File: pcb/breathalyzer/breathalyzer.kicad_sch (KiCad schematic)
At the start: 29 parts, among them J1 Conn_01x07_Pin, J2 MP-3B socket, Q1 Q_PMOS, Q2 NPN, SW1 PTS636SK43SMTR, SW2 430162085826, U1 STM32F030K6Tx, U2 TLV73325PDBV, U4 TLV61070ADBV, U5 AY0438X-L

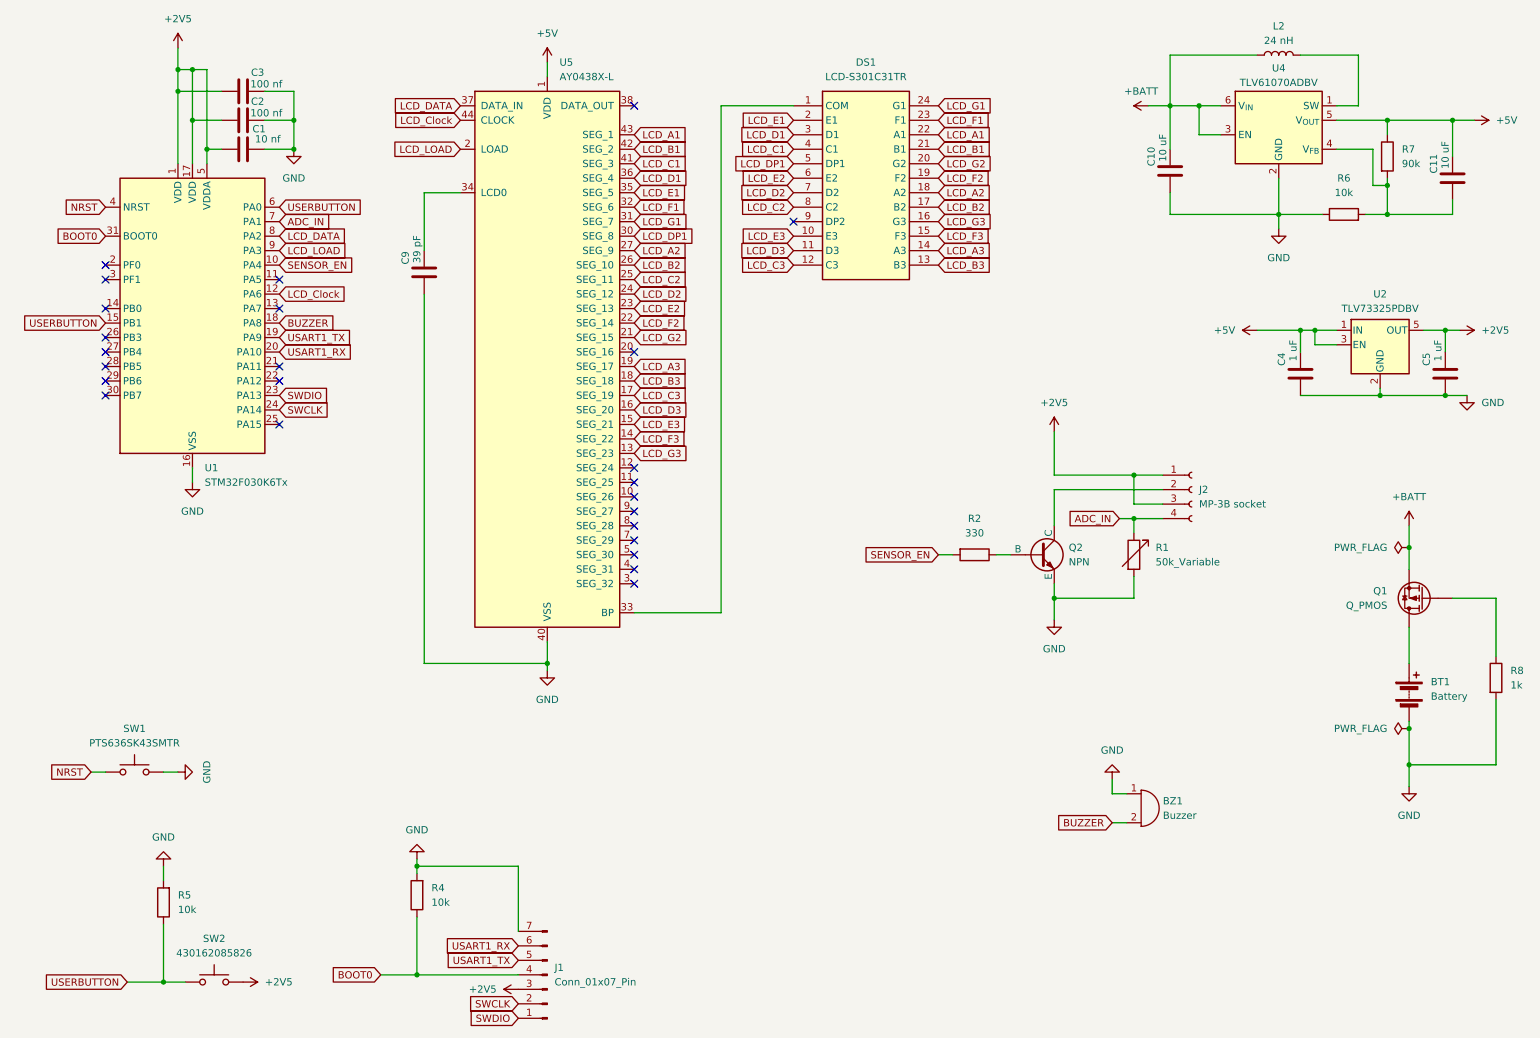
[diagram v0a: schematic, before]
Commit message: update from schematic
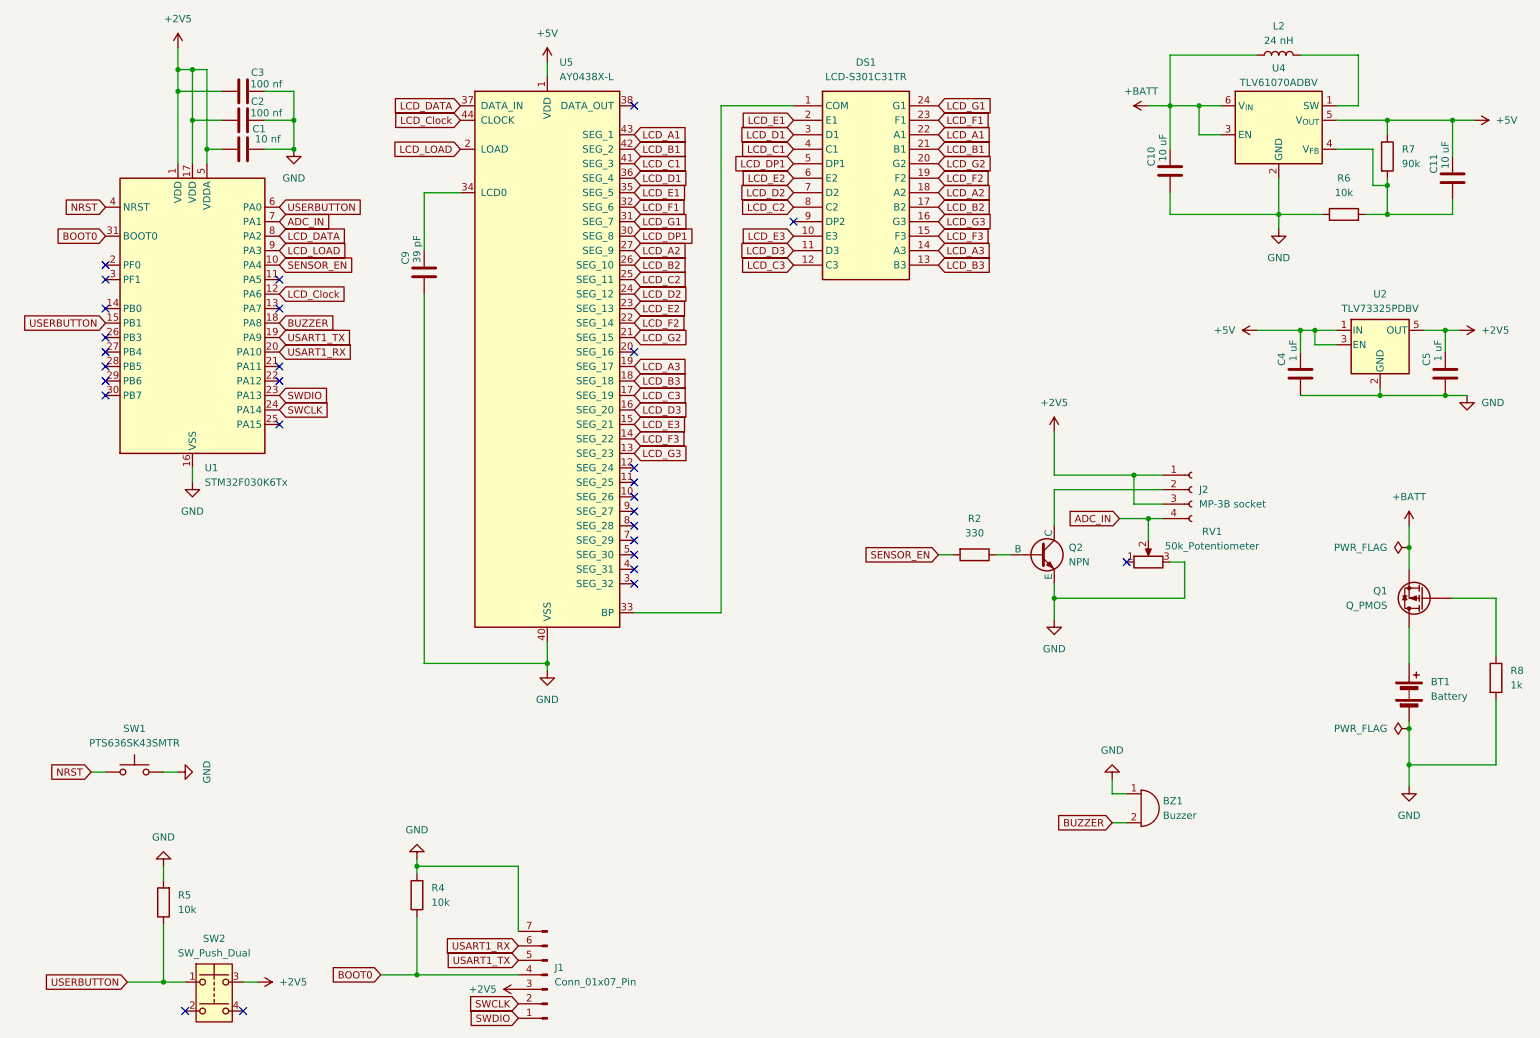
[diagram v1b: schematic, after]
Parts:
- removed R1: 50k_Variable, Potentiometer_THT:Potentiometer_ACP_CA9-H5_Horizontal, symbol Device:R_Variable
- removed SW2: 430162085826, breathalyzer:430162085826, symbol Switch:SW_Push
- added RV1: 50k_Potentiometer, Potentiometer_THT:Potentiometer_ACP_CA9-H5_Horizontal, symbol Device:R_Potentiometer
- added SW2: SW_Push_Dual, breathalyzer:430162085826, symbol Switch:SW_Push_Dual
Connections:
- net +2V5: now also SW2.3
- net ADC_IN: now also RV1.2
- net GND: now also RV1.3
- net USERBUTTON: now also SW2.1
- no-connect marks 25 -> 28
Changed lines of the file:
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@@
 	)
 	(junction
-		(at 209.55 101.6)
-		(diameter 0)
-		(color 0 0 0 0)
-	)
-	(junction
 		(at 254 48.26)
 		(diameter 0)
@@
 		(color 0 0 0 0)
 	)
+	(junction
+		(at 212.09 101.6)
+		(diameter 0)
+		(color 0 0 0 0)
+	)
 	(no_connect
 		(at 121.92 110.49)
@@
 	)
 	(no_connect
+		(at 208.28 109.22)
+	)
+	(no_connect
 		(at 121.92 113.03)
 	)
@@
 	)
 	(no_connect
+		(at 43.18 187.96)
+	)
+	(no_connect
 		(at 59.69 85.09)
 	)
@@
 	)
 	(no_connect
+		(at 53.34 187.96)
+	)
+	(no_connect
 		(at 29.21 74.93)
 	)
@@
 	(wire
 		(pts
+			(xy 218.44 109.22) (xy 218.44 115.57)
+		)
+		(stroke
+			(width 0)
+			(type default)
+		)
+	)
+	(wire
+		(pts
 			(xy 46.99 36.83) (xy 49.53 36.83)
 		)
@@
 	(wire
 		(pts
-			(xy 214.63 101.6) (xy 209.55 101.6)
+			(xy 207.01 101.6) (xy 212.09 101.6)
 		)
 		(stroke
@@
 	(wire
 		(pts
-			(xy 209.55 101.6) (xy 209.55 104.14)
+			(xy 252.73 78.74) (xy 252.73 80.01)
 		)
 		(stroke
@@
 	(wire
 		(pts
-			(xy 252.73 78.74) (xy 252.73 80.01)
+			(xy 44.45 95.25) (xy 44.45 92.71)
 		)
 		(stroke
@@
 	(wire
 		(pts
-			(xy 44.45 95.25) (xy 44.45 92.71)
+			(xy 266.7 68.58) (xy 264.16 68.58)
 		)
 		(stroke
@@
 	(wire
 		(pts
-			(xy 266.7 68.58) (xy 264.16 68.58)
+			(xy 220.98 34.29) (xy 220.98 29.21)
 		)
 		(stroke
@@
 	(wire
 		(pts
-			(xy 220.98 34.29) (xy 220.98 29.21)
+			(xy 62.23 31.75) (xy 62.23 36.83)
 		)
 		(stroke
@@
 	(wire
 		(pts
-			(xy 62.23 31.75) (xy 62.23 36.83)
+			(xy 212.09 101.6) (xy 214.63 101.6)
 		)
 		(stroke
@@
 	(wire
 		(pts
-			(xy 44.45 31.75) (xy 44.45 39.37)
+			(xy 55.88 182.88) (xy 53.34 182.88)
 		)
 		(stroke
@@
 	(wire
 		(pts
-			(xy 41.91 22.86) (xy 41.91 26.67)
+			(xy 44.45 31.75) (xy 44.45 39.37)
 		)
 		(stroke
@@
 	(wire
 		(pts
-			(xy 83.82 162.56) (xy 101.6 162.56)
+			(xy 218.44 109.22) (xy 215.9 109.22)
 		)
 		(stroke
@@
 	(wire
 		(pts
-			(xy 241.3 71.12) (xy 241.3 68.58)
+			(xy 41.91 22.86) (xy 41.91 26.67)
 		)
 		(stroke
@@
 	(wire
 		(pts
-			(xy 205.74 149.86) (xy 208.28 149.86)
+			(xy 83.82 162.56) (xy 101.6 162.56)
 		)
 		(stroke
@@
 	(wire
 		(pts
-			(xy 39.37 182.88) (xy 43.18 182.88)
+			(xy 241.3 71.12) (xy 241.3 68.58)
 		)
 		(stroke
@@
 	(wire
 		(pts
-			(xy 209.55 111.76) (xy 209.55 115.57)
+			(xy 205.74 149.86) (xy 208.28 149.86)
 		)
 		(stroke
@@
 	(wire
 		(pts
-			(xy 83.82 161.29) (xy 83.82 162.56)
+			(xy 39.37 182.88) (xy 43.18 182.88)
 		)
 		(stroke
@@
 	(wire
 		(pts
-			(xy 209.55 115.57) (xy 195.58 115.57)
+			(xy 83.82 161.29) (xy 83.82 162.56)
 		)
 		(stroke
@@
 	(wire
 		(pts
-			(xy 195.58 115.57) (xy 195.58 119.38)
+			(xy 195.58 115.57) (xy 218.44 115.57)
 		)
 		(stroke
@@
 	(wire
 		(pts
-			(xy 207.01 101.6) (xy 209.55 101.6)
+			(xy 195.58 115.57) (xy 195.58 119.38)
 		)
 		(stroke
@@
 	(wire
 		(pts
+			(xy 212.09 101.6) (xy 212.09 105.41)
+		)
+		(stroke
+			(width 0)
+			(type default)
+		)
+	)
+	(wire
+		(pts
 			(xy 62.23 26.67) (xy 62.23 31.75)
 		)
@@
 	(symbol
 		(lib_id "power:+2V5")
-		(at 53.34 182.88 270)
+		(at 55.88 182.88 270)
 		(unit 1)
 		(exclude_from_sim no)
@@
 		(fields_autoplaced yes)
 		(property "Reference" "#PWR010"
-			(at 49.53 182.88 0)
+			(at 52.07 182.88 0)
 			(effects
 				(font
@@
 		)
 		(property "Value" "+2V5"
-			(at 57.15 182.8799 90)
+			(at 59.69 182.8799 90)
 			(effects
 				(font
@@
 		)
 		(property "Footprint" ""
-			(at 53.34 182.88 0)
+			(at 55.88 182.88 0)
 			(effects
 				(font
@@
 		)
 		(property "Datasheet" ""
-			(at 53.34 182.88 0)
+			(at 55.88 182.88 0)
 			(effects
 				(font
@@
 		)
 		(property "Description" "Power symbol creates a global label with name \"+2V5\""
-			(at 53.34 182.88 0)
+			(at 55.88 182.88 0)
 			(effects
 				(font
@@
 	)
 	(symbol
-		(lib_name "SW_Push_1")
-		(lib_id "Switch:SW_Push")
-		(at 48.26 182.88 0)
+		(lib_id "Device:R_Potentiometer")
+		(at 212.09 109.22 90)
 		(unit 1)
 		(exclude_from_sim no)
@@
 		(on_board yes)
 		(dnp no)
-		(fields_autoplaced yes)
-		(property "Reference" "SW2"
-			(at 48.26 175.26 0)
+		(property "Reference" "RV1"
+			(at 223.266 103.886 90)
 			(effects
 				(font
@@
 			)
 		)
-		(property "Value" "430162085826"
-			(at 48.26 177.8 0)
+		(property "Value" "50k_Potentiometer"
+			(at 223.266 106.426 90)
 			(effects
 				(font
@@
 			)
 		)
-		(property "Footprint" "breathalyzer:430162085826"
-			(at 48.26 177.8 0)
+		(property "Footprint" "Potentiometer_THT:Potentiometer_ACP_CA9-H5_Horizontal"
+			(at 212.09 109.22 0)
 			(effects
 				(font
@@
 			)
 		)
-		(property "Datasheet" "https://hu.mouser.com/ProductDetail/Wurth-Elektronik/430162085826?qs=sPbYRqrBIVnNOZ1%252Bx8%2F2Rw%3D%3D"
-			(at 48.26 177.8 0)
+		(property "Datasheet" "https://hu.mouser.com/ProductDetail/Same-Sky/PTN06-B50CB20-H?qs=sGAEpiMZZMu7u4aXTvZ%252Bj76JCkJt%2F1Rf8NnkN%252BqUlJ17HNc3pPYO6w%3D%3D"
+			(at 212.09 109.22 0)
 			(effects
 				(font
@@
 			)
 		)
-		(property "Description" "Push button switch, generic, two pins"
-			(at 48.26 182.88 0)
+		(property "Description" "Potentiometer"
+			(at 212.09 109.22 0)
 			(effects
 				(font
@@
 			)
 		)
-		(pin "3"
-		)
 		(pin "1"
 		)
+		(pin "2"
+		)
+		(pin "3"
+		)
 		(instances
-			(project "breathalyzer"
+			(project ""
 				(path "/e92d6a20-f7e6-42bc-b7eb-52ddd833ed75"
-					(reference "SW2")
+					(reference "RV1")
 					(unit 1)
 				)
@@
 	)
 	(symbol
+		(lib_id "Switch:SW_Push_Dual")
+		(at 48.26 185.42 0)
+		(unit 1)
+		(exclude_from_sim no)
+		(in_bom yes)
+		(on_board yes)
+		(dnp no)
+		(fields_autoplaced yes)
+		(property "Reference" "SW2"
+			(at 48.26 175.26 0)
+			(effects
+				(font
+					(size 1.27 1.27)
+				)
+			)
+		)
+		(property "Value" "SW_Push_Dual"
+			(at 48.26 177.8 0)
+			(effects
+				(font
+					(size 1.27 1.27)
+				)
+			)
+		)
+		(property "Footprint" "breathalyzer:430162085826"
+			(at 48.26 177.8 0)
+			(effects
+				(font
+					(size 1.27 1.27)
+				)
+				(hide yes)
+			)
+		)
+		(property "Datasheet" "https://hu.mouser.com/ProductDetail/Wurth-Elektronik/430162085826?qs=sPbYRqrBIVnNOZ1%252Bx8%2F2Rw%3D%3D"
+			(at 48.26 185.42 0)
+			(effects
+				(font
+					(size 1.27 1.27)
+				)
+				(hide yes)
+			)
+		)
+		(property "Description" "Push button switch, generic, symbol, four pins"
+			(at 48.26 185.42 0)
+			(effects
+				(font
+					(size 1.27 1.27)
+				)
+				(hide yes)
+			)
+		)
+		(pin "2"
+		)
+		(pin "4"
+		)
+		(pin "1"
+		)
+		(pin "3"
+		)
+		(instances
+			(project ""
+				(path "/e92d6a20-f7e6-42bc-b7eb-52ddd833ed75"
+					(reference "SW2")
+					(unit 1)
+				)
+			)
+		)
+	)
+	(symbol
 		(lib_id "power:+5V")
 		(at 269.24 31.75 270)
@@
 					(unit 1)
 				)
-			)
-		)
-	)
-	(symbol
-		(lib_id "Device:R_Variable")
-		(at 209.55 107.95 0)
-		(unit 1)
-		(exclude_from_sim no)
-		(in_bom yes)
-		(on_board yes)
-		(dnp no)
-		(fields_autoplaced yes)
-		(property "Reference" "R1"
-			(at 213.36 106.6799 0)
-			(effects
-				(font
-					(size 1.27 1.27)
-				)
-				(justify left)
-			)
-		)
-		(property "Value" "50k_Variable"
-			(at 213.36 109.2199 0)
-			(effects
-				(font
-					(size 1.27 1.27)
-				)
-				(justify left)
-			)
-		)
-		(property "Footprint" "Potentiometer_THT:Potentiometer_ACP_CA9-H5_Horizontal"
-			(at 207.772 107.95 90)
-			(effects
-				(font
-					(size 1.27 1.27)
-				)
-				(hide yes)
-			)
-		)
-		(property "Datasheet" "https://hu.mouser.com/ProductDetail/Same-Sky/PTN06-B50CB20-H?qs=sGAEpiMZZMu7u4aXTvZ%252Bj76JCkJt%2F1Rf8NnkN%252BqUlJ17HNc3pPYO6w%3D%3D"
-			(at 209.55 107.95 0)
-			(effects
-				(font
-					(size 1.27 1.27)
-				)
-				(hide yes)
-			)
-		)
-		(property "Description" "Variable resistor"
-			(at 209.55 107.95 0)
-			(effects
-				(font
-					(size 1.27 1.27)
-				)
-				(hide yes)
-			)
-		)
-		(pin "2"
-		)
-		(pin "1"
-		)
-		(instances
-			(project ""
-				(path "/e92d6a20-f7e6-42bc-b7eb-52ddd833ed75"
-					(reference "R1")
-					(unit 1)
-				)

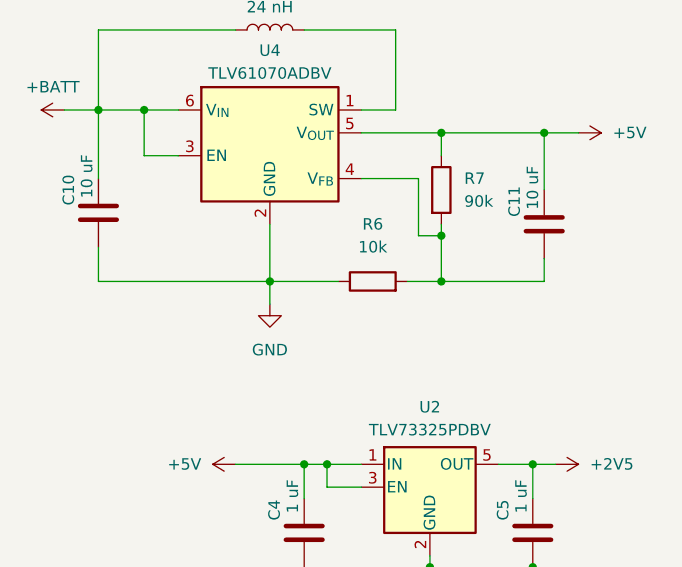
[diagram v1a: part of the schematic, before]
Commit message: 5V fix
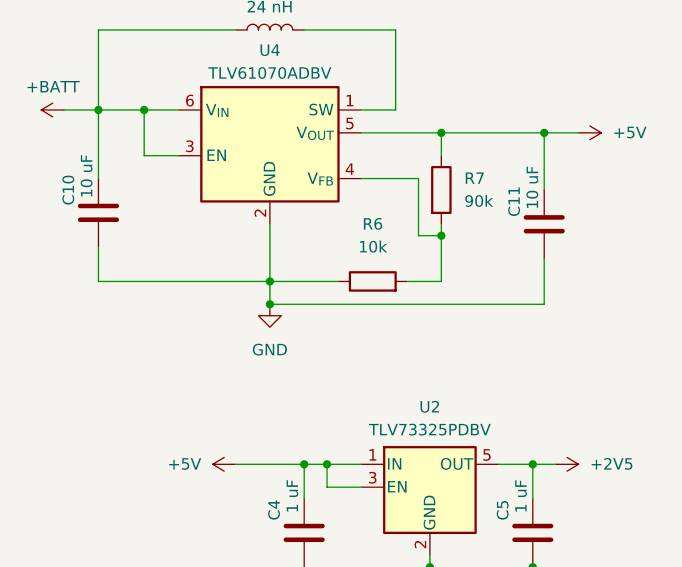
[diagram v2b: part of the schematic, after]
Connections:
- net GND: now also C11.1
- net at R6.2, R7.2, U4.4 (V_{FB}): no longer C11.1
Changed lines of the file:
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@@
+	)
+	(junction
+		(at 234.95 50.8)
+		(diameter 0)
+		(color 0 0 0 0)
 	)
 	(junction
@@
 	)
 	(junction
-		(at 254 48.26)
-		(diameter 0)
-		(color 0 0 0 0)
-	)
-	(junction
 		(at 252.73 80.01)
 		(diameter 0)
@@
 	(wire
 		(pts
+			(xy 265.43 45.72) (xy 265.43 50.8)
+		)
+		(stroke
+			(width 0)
+			(type default)
+		)
+	)
+	(wire
+		(pts
 			(xy 44.45 31.75) (xy 44.45 39.37)
 		)
@@
 	(wire
 		(pts
-			(xy 265.43 48.26) (xy 254 48.26)
-		)
-		(stroke
-			(width 0)
-			(type default)
-		)
-	)
-	(wire
-		(pts
 			(xy 57.15 26.67) (xy 62.23 26.67)
 		)
@@
 	(wire
 		(pts
+			(xy 265.43 50.8) (xy 234.95 50.8)
+		)
+		(stroke
+			(width 0)
+			(type default)
+		)
+	)
+	(wire
+		(pts
 			(xy 205.74 147.32) (xy 205.74 149.86)
 		)
@@
 		)
 		(stroke
-			(width 0)
-			(type default)
-		)
-	)
-	(wire
-		(pts
-			(xy 265.43 45.72) (xy 265.43 48.26)
-		)
-		(stroke

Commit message: layout correction
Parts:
- BT1: value Battery -> 2x AA Battery
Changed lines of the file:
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@@
 		(on_board yes)
 		(dnp no)
-		(fields_autoplaced yes)
 		(property "Reference" "BT1"
 			(at 261.62 130.2384 0)
@@
 			)
 		)
-		(property "Value" "Battery"
-			(at 261.62 132.7784 0)
+		(property "Value" "2x AA Battery"
+			(at 259.588 132.842 0)
 			(effects
 				(font
